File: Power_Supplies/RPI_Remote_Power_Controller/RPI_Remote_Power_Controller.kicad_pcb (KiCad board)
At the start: 2 copper layers, 234.9 x 103.5 mm, 36 parts, among them J1 Screw_Terminal_01x02, J10 Screw_Terminal_01x03, J11 Raspberry_Pi_Zero_W, J12 Screw_Terminal_01x02, J2 Screw_Terminal_01x02, J3 Screw_Terminal_01x02, J4 Screw_Terminal_01x02, J5 Screw_Terminal_01x02, J6 Screw_Terminal_01x02, J7 Screw_Terminal_01x02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

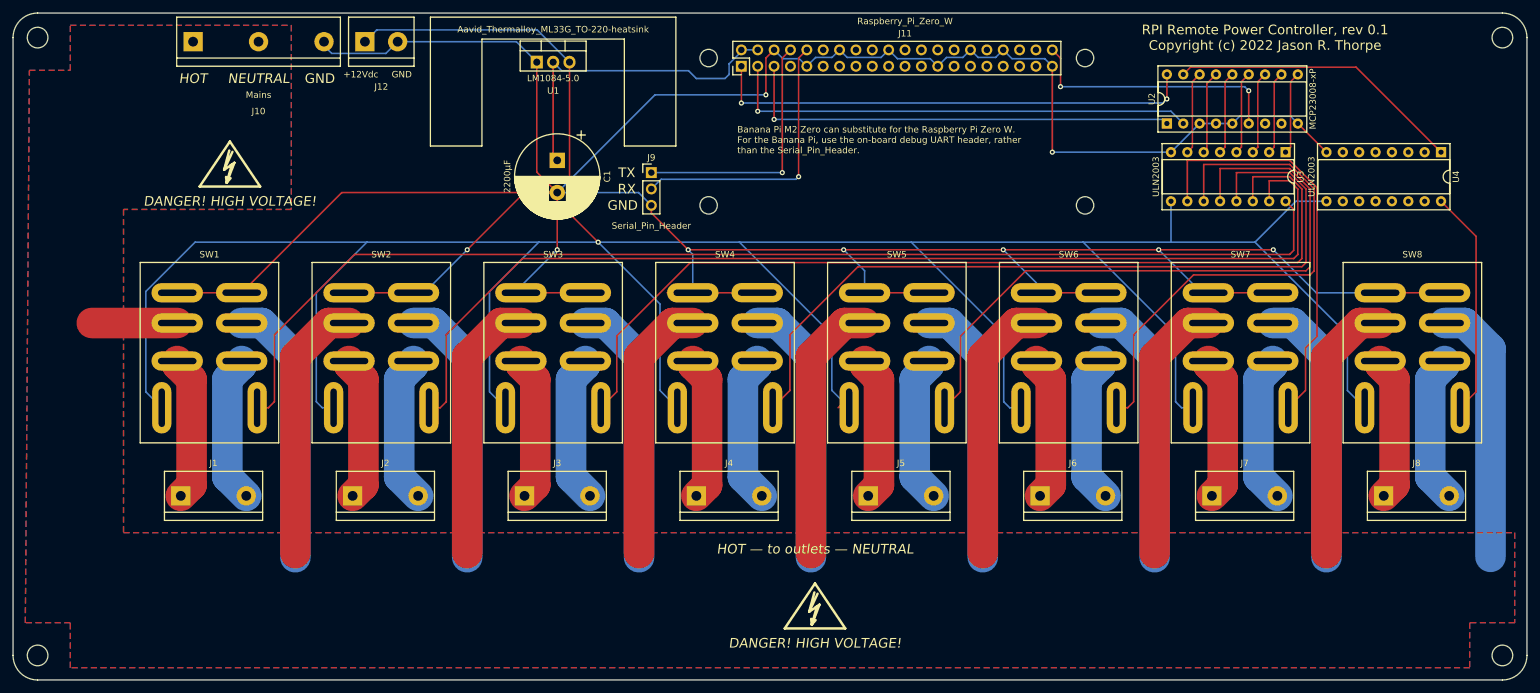
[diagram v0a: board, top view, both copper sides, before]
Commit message: Increase trace clarance for the default net class to 0.3mm, and reroute several traces to meet new clearance requirements.
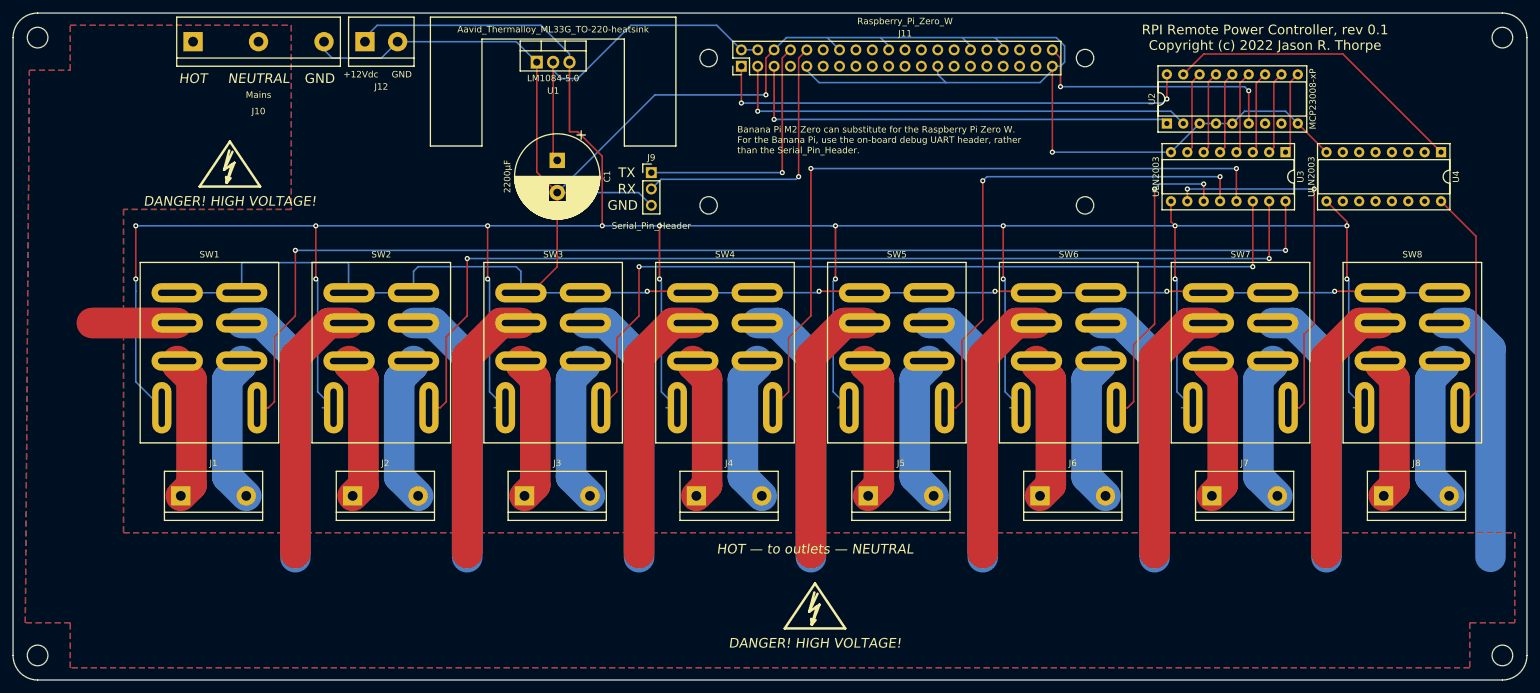
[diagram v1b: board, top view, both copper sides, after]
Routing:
- net GND: track 572.4 -> 532.0 mm, vias 9 -> 7
- net Net-(SW6-Pad8): track 82.7 -> 48.1 mm, vias 0 -> 2
- net Net-(SW5-Pad8): track 103.3 -> 79.6 mm, vias 0 -> 2
- net Net-(SW3-Pad8): track 146.5 -> 129.8 mm, vias 0 -> 2
- net Net-(SW4-Pad8): track 124.9 -> 110.7 mm, vias 0 -> 2
- net Net-(SW2-Pad8): track 169.3 -> 160.2 mm, vias 0 -> 2
- net +12V: track 507.0 -> 513.6 mm, vias 1 -> 17
- net Net-(SW7-Pad8): track 64.2 -> 58.2 mm, vias 0 -> 2
- net Net-(SW1-Pad8): track 185.2 -> 189.2 mm, vias 0 -> 2
- net +5V: track 51.5 -> 54.6 mm
- net Net-(U2-Pad17): track 45.9 -> 47.6 mm
- net Net-(U2-Pad15): track 12.9 -> 13.5 mm
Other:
- net class Default: clearance 0.2 -> 0.25
- rule trace_clearance: 0.2 -> 0.25
